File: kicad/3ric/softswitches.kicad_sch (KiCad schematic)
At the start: 11 parts

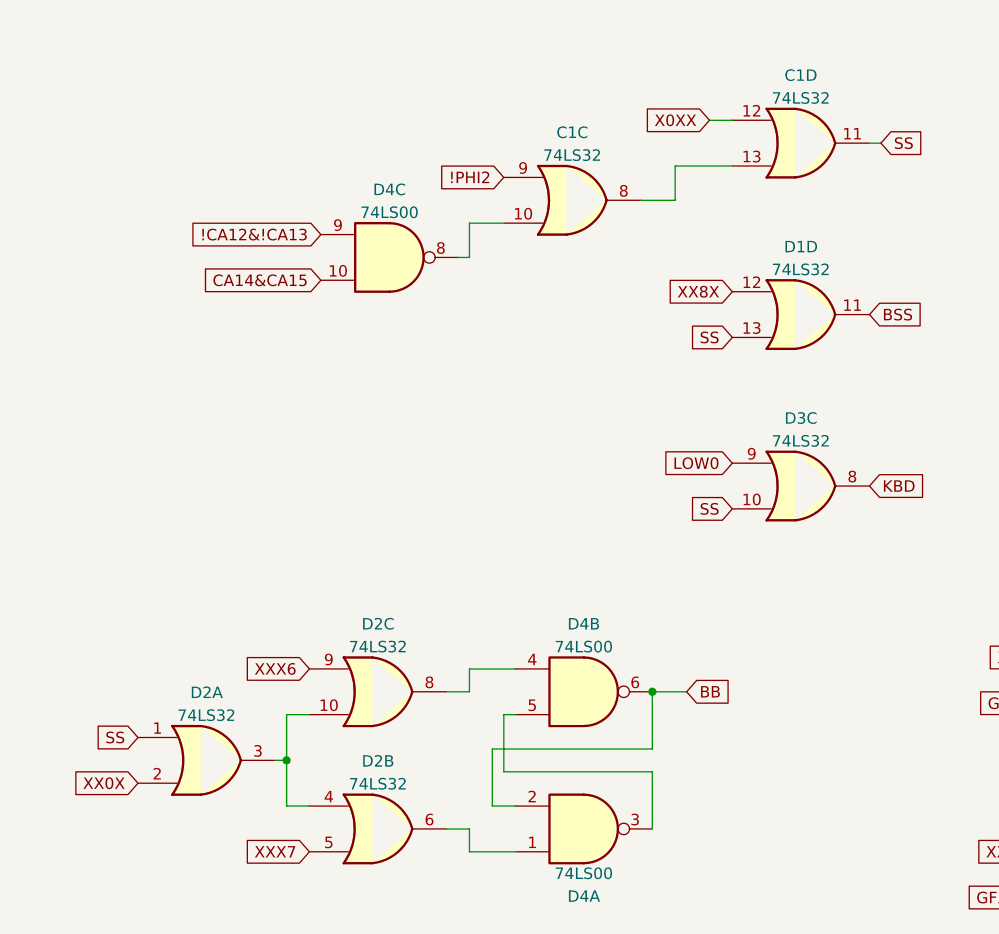
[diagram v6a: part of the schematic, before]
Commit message: update schematic with corrections found via virutal wiring
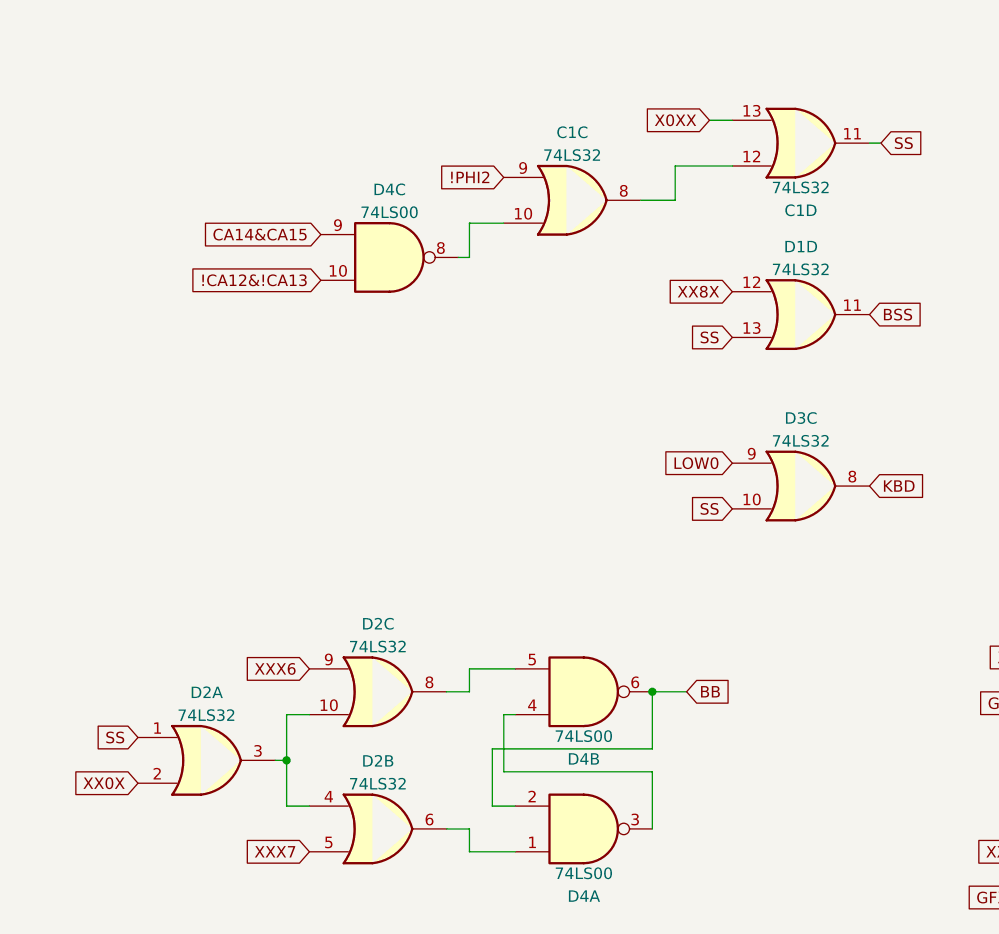
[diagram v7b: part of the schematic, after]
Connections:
- net !CA12&!CA13: now also D4.10; no longer D4.9
- net CA14&CA15: now also D4.9; no longer D4.10
- net X0XX: now also C1.13; no longer C1.12
- net at D2.8: now also D4.5; no longer D4.4
- net at D4.3: now also D4.4; no longer D4.5
- net at C1.8: now also C1.12; no longer C1.13
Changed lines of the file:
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@@
 		)
 	)
-	(global_label "CA14&CA15"
-		(shape input)
-		(at 67.31 45.72 180)
-		(fields_autoplaced yes)
-		(effects
-			(font
-				(size 1.27 1.27)
-			)
-			(justify right)
-		)
-		(property "Intersheetrefs" "${INTERSHEET_REFS}"
-			(at 53.1972 45.72 0)
-			(effects
-				(font
-					(size 1.27 1.27)
-				)
-				(justify right)
-				(hide yes)
-			)
-		)
-	)
 	(global_label "XXX4"
 		(shape input)
@@
 		)
 	)
+	(global_label "!CA12&!CA13"
+		(shape input)
+		(at 67.31 45.72 180)
+		(fields_autoplaced yes)
+		(effects
+			(font
+				(size 1.27 1.27)
+			)
+			(justify right)
+		)
+		(property "Intersheetrefs" "${INTERSHEET_REFS}"
+			(at 51.9876 45.72 0)
+			(effects
+				(font
+					(size 1.27 1.27)
+				)
+				(justify right)
+				(hide yes)
+			)
+		)
+	)
 	(global_label "XX7X"
 		(shape input)
@@
 		)
 	)
+	(global_label "CA14&CA15"
+		(shape input)
+		(at 67.31 40.64 180)
+		(fields_autoplaced yes)
+		(effects
+			(font
+				(size 1.27 1.27)
+			)
+			(justify right)
+		)
+		(property "Intersheetrefs" "${INTERSHEET_REFS}"
+			(at 53.1972 40.64 0)
+			(effects
+				(font
+					(size 1.27 1.27)
+				)
+				(justify right)
+				(hide yes)
+			)
+		)
+	)
 	(global_label "LOW0"
 		(shape input)
@@
 		)
 	)
-	(global_label "!CA12&!CA13"
-		(shape input)
-		(at 67.31 40.64 180)
-		(fields_autoplaced yes)
-		(effects
-			(font
-				(size 1.27 1.27)
-			)
-			(justify right)
-		)
-		(property "Intersheetrefs" "${INTERSHEET_REFS}"
-			(at 51.9876 40.64 0)
-			(effects
-				(font
-					(size 1.27 1.27)
-				)
-				(justify right)
-				(hide yes)
-			)
-		)
-	)
 	(global_label "XX1X"
 		(shape input)
@@
 		(lib_id "74xx:74LS00")
 		(at 96.52 91.44 0)
+		(mirror x)
 		(unit 2)
 		(exclude_from_sim no)
@@
 		(on_board yes)
 		(dnp no)
-		(fields_autoplaced yes)
 		(property "Reference" "D4"
-			(at 96.52 83.9302 0)
+			(at 96.52 98.9498 0)
 			(effects
 				(font
@@
 		)
 		(property "Value" "74LS00"
-			(at 96.52 86.4671 0)
+			(at 96.52 96.4129 0)
 			(effects
 				(font
@@
 		(lib_id "74xx:74LS32")
 		(at 120.65 30.48 0)
+		(mirror x)
 		(unit 4)
 		(exclude_from_sim no)
@@
 		(on_board yes)
 		(dnp no)
-		(fields_autoplaced yes)
 		(property "Reference" "C1"
-			(at 120.65 22.9702 0)
+			(at 120.65 37.9898 0)
 			(effects
 				(font
@@
 		)
 		(property "Value" "74LS32"
-			(at 120.65 25.5071 0)
+			(at 120.65 35.4529 0)
 			(effects
 				(font

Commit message: cleaning up of the schematic
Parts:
- added unit 2 of C1
- added unit 4 of D4
- C1, D1, D2, D3, D4, E3, E4, E5, E6: footprint (none) -> Package_DIP:DIP-14_W7.62mm_Socket
- D5, D6: footprint (none) -> Package_DIP:DIP-24_W15.24mm_Socket
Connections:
- net LOW0: no longer D3.9
- net SS: no longer D3.10, D3.13
- net JOYSS: no longer names the net of D3.11
- net KBD: no longer names the net of D3.8
- net XX6X: no longer names the net of D6.7 (S6)
- net XX6X: no longer D3.12
- no-connect marks 0 -> 25
